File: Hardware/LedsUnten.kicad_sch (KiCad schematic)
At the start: 27 parts

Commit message: assign remaining LCSC numbers and change R_sense of LED drivers
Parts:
- added R9: 0.5, Resistor_SMD:R_0805_2012Metric, symbol Device:R_Small
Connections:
- net GND: now also R9.2
- new net LedTreiber4/R_{sense}: R9.1
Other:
- sheet LedTreiber4 ports: added R_{sense}; removed none
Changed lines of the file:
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@@
 	(wire
 		(pts
-			(xy 88.9 116.84) (xy 201.93 116.84)
+			(xy 95.25 116.84) (xy 201.93 116.84)
 		)
 		(stroke
@@
 	(wire
 		(pts
-			(xy 74.93 97.79) (xy 88.9 97.79)
+			(xy 74.93 93.98) (xy 95.25 93.98)
 		)
 		(stroke
@@
 	(wire
 		(pts
-			(xy 88.9 97.79) (xy 88.9 116.84)
+			(xy 95.25 93.98) (xy 95.25 116.84)
 		)
 		(stroke
@@
 	(wire
 		(pts
-			(xy 105.41 76.2) (xy 105.41 90.17)
+			(xy 74.93 97.79) (xy 87.63 97.79)
 		)
 		(stroke
@@
 		)
 	)
+	(wire
+		(pts
+			(xy 105.41 76.2) (xy 105.41 90.17)
+		)
+		(stroke
+			(width 0)
+			(type default)
+		)
+	)
 	(global_label "WhiteDim"
 		(shape input)
@@
 	)
 	(symbol
+		(lib_id "Device:R_Small")
+		(at 87.63 100.33 0)
+		(unit 1)
+		(exclude_from_sim no)
+		(in_bom yes)
+		(on_board yes)
+		(dnp no)
+		(fields_autoplaced yes)
+		(property "Reference" "R9"
+			(at 90.17 99.0599 0)
+			(effects
+				(font
+					(size 1.27 1.27)
+				)
+				(justify left)
+			)
+		)
+		(property "Value" "0.5"
+			(at 90.17 101.5999 0)
+			(effects
+				(font
+					(size 1.27 1.27)
+				)
+				(justify left)
+			)
+		)
+		(property "Footprint" "Resistor_SMD:R_0805_2012Metric"
+			(at 87.63 100.33 0)
+			(effects
+				(font
+					(size 1.27 1.27)
+				)
+				(hide yes)
+			)
+		)
+		(property "Datasheet" "~"
+			(at 87.63 100.33 0)
+			(effects
+				(font
+					(size 1.27 1.27)
+				)
+				(hide yes)
+			)
+		)
+		(property "Description" "Resistor, small symbol"
+			(at 87.63 100.33 0)
+			(effects
+				(font
+					(size 1.27 1.27)
+				)
+				(hide yes)
+			)
+		)
+		(pin "1"
+		)
+		(pin "2"
+		)
+		(instances
+			(project "LEDTischLampe"
+				(path "/34c772aa-2c68-48ca-93c3-7ad335c6d96d/5ca28fd6-5d3d-44e4-a7e8-e548f0114941"
+					(reference "R9")
+					(unit 1)
+				)
+			)
+		)
+	)
+	(symbol
+		(lib_id "power:GND")
+		(at 87.63 102.87 0)
+		(unit 1)
+		(exclude_from_sim no)
+		(in_bom yes)
+		(on_board yes)
+		(dnp no)
+		(property "Reference" "#PWR025"
+			(at 87.63 109.22 0)
+			(effects
+				(font
+					(size 1.27 1.27)
+				)
+				(hide yes)
+			)
+		)
+		(property "Value" "GND"
+			(at 87.63 106.426 0)
+			(effects
+				(font
+					(size 1.27 1.27)
+				)
+			)
+		)
+		(property "Footprint" ""
+			(at 87.63 102.87 0)
+			(effects
+				(font
+					(size 1.27 1.27)
+				)
+				(hide yes)
+			)
+		)
+		(property "Datasheet" ""
+			(at 87.63 102.87 0)
+			(effects
+				(font
+					(size 1.27 1.27)
+				)
+				(hide yes)
+			)
+		)
+		(property "Description" ""
+			(at 87.63 102.87 0)
+			(effects
+				(font
+					(size 1.27 1.27)
+				)
+				(hide yes)
+			)
+		)
+		(pin "1"
+		)
+		(instances
+			(project "LEDTischLampe"
+				(path "/34c772aa-2c68-48ca-93c3-7ad335c6d96d/5ca28fd6-5d3d-44e4-a7e8-e548f0114941"
+					(reference "#PWR025")
+					(unit 1)
+				)
+			)
+		)
+	)
+	(symbol
 		(lib_id "Device:R")
 		(at 111.76 104.14 90)
@@
 		)
 		(pin "LEDN" input
-			(at 74.93 97.79 0)
+			(at 74.93 93.98 0)
 			(effects
 				(font
@@
 			)
 		)
+		(pin "R_{sense}" input
+			(at 74.93 97.79 0)
+			(effects
+				(font
+					(size 1.27 1.27)
+				)
+				(justify right)
+			)
+		)

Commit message: remove LCSC numbers from silkscreen (bug in jlcpcb-tools)
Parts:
- LED1, LED10, LED11, LED12, LED13, LED14, LED15, LED16, LED17, LED18, LED19, LED2, LED20, LED21, LED22, LED23, LED24, LED3, LED4, LED5, LED6, LED7, LED8, LED9: LCSC (none) -> C210320
- R5, R6, R7: LCSC (none) -> C17415
- R9: LCSC (none) -> C2930328

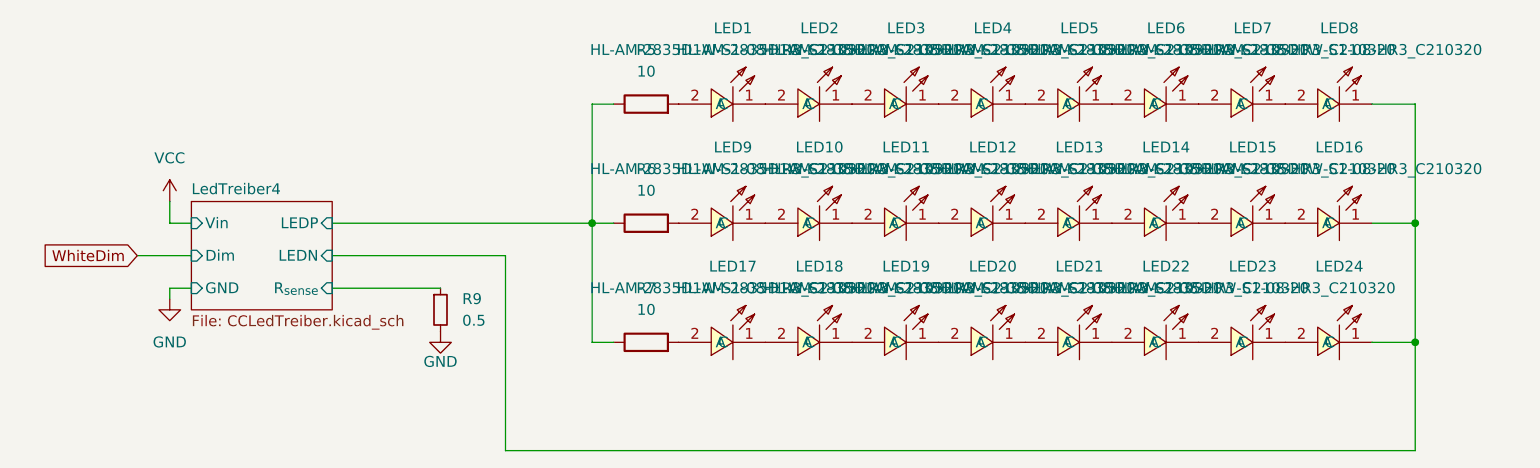
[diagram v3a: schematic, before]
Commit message: some fixes and BOM optimization, heatsinking, etc
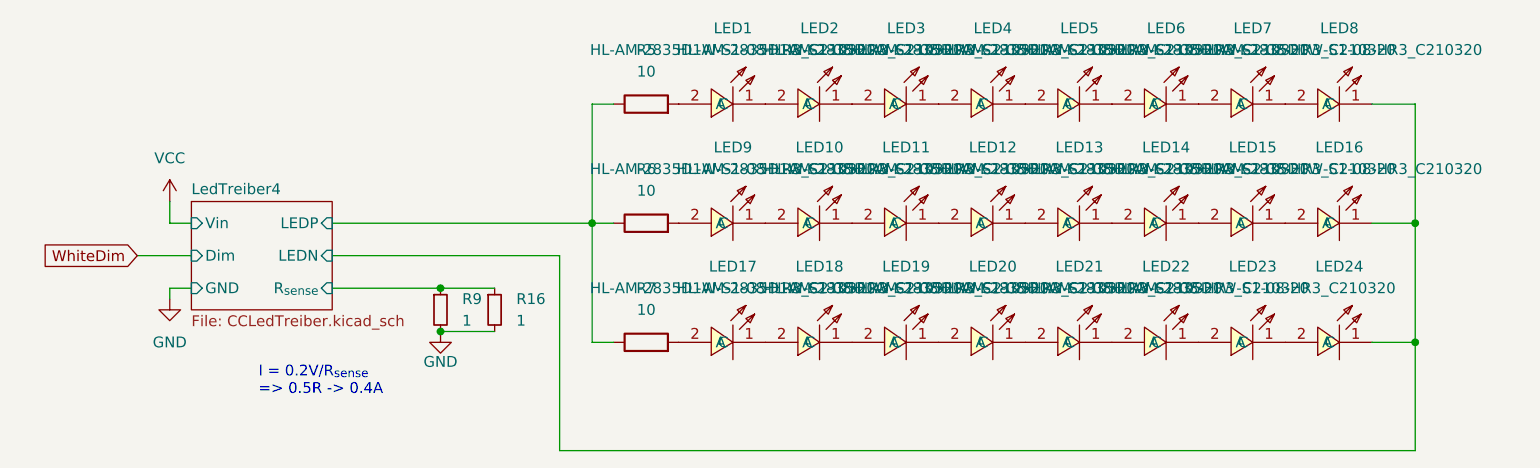
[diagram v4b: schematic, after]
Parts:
- added R16: 1, Resistor_SMD:R_0805_2012Metric, symbol Device:R_Small
- R9: value 0.5 -> 1; LCSC C2930328 -> C25271
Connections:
- net GND: now also R16.2
- net LedTreiber4/R_{sense}: now also R16.1
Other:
- note added: "I = 0.2V/R_{sense} => 0.5R -> 0.4A"
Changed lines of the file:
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@@
 		(color 0 0 0 0)
 	)
+	(junction
+		(at 87.63 102.87)
+		(diameter 0)
+		(color 0 0 0 0)
+	)
+	(junction
+		(at 87.63 97.79)
+		(diameter 0)
+		(color 0 0 0 0)
+	)
 	(wire
 		(pts
@@
 	(wire
 		(pts
-			(xy 95.25 116.84) (xy 201.93 116.84)
+			(xy 101.6 116.84) (xy 201.93 116.84)
 		)
 		(stroke
@@
 	(wire
 		(pts
+			(xy 87.63 97.79) (xy 93.98 97.79)
+		)
+		(stroke
+			(width 0)
+			(type default)
+		)
+	)
+	(wire
+		(pts
 			(xy 55.88 87.63) (xy 55.88 90.17)
 		)
@@
 	(wire
 		(pts
-			(xy 74.93 93.98) (xy 95.25 93.98)
+			(xy 74.93 93.98) (xy 101.6 93.98)
 		)
 		(stroke
@@
 	(wire
 		(pts
-			(xy 95.25 93.98) (xy 95.25 116.84)
+			(xy 101.6 93.98) (xy 101.6 116.84)
 		)
 		(stroke
@@
 	(wire
 		(pts
+			(xy 87.63 102.87) (xy 93.98 102.87)
+		)
+		(stroke
+			(width 0)
+			(type default)
+		)
+	)
+	(wire
+		(pts
 			(xy 201.93 104.14) (xy 201.93 90.17)
 		)
@@
 			(width 0)
 			(type default)
+		)
+	)
+	(text "I = 0.2V/R_{sense}\n=> 0.5R -> 0.4A"
+		(exclude_from_sim no)
+		(at 66.294 108.712 0)
+		(effects
+			(font
+				(size 1.27 1.27)
+			)
+			(justify left)
 		)
 	)
@@
 			)
 		)
-		(property "Value" "0.5"
+		(property "Value" "1"
 			(at 90.17 101.5999 0)
 			(effects
@@
 			)
 		)
-		(property "LCSC" "C2930328"
+		(property "LCSC" "C25271"
 			(at 90.17 99.0599 0)
 			(effects
@@
 					(unit 1)
 				)
+			)
+		)
+	)
+	(symbol
+		(lib_id "Device:R_Small")
+		(at 93.98 100.33 0)
+		(unit 1)
+		(exclude_from_sim no)
+		(in_bom yes)
+		(on_board yes)
+		(dnp no)
+		(fields_autoplaced yes)
+		(property "Reference" "R16"
+			(at 96.52 99.0599 0)
+			(effects
+				(font
+					(size 1.27 1.27)
+				)
+				(justify left)
+			)
+		)
+		(property "Value" "1"
+			(at 96.52 101.5999 0)
+			(effects
+				(font
+					(size 1.27 1.27)
+				)
+				(justify left)
+			)
+		)
+		(property "Footprint" "Resistor_SMD:R_0805_2012Metric"
+			(at 93.98 100.33 0)
+			(effects
+				(font
+					(size 1.27 1.27)
+				)
+				(hide yes)
+			)
+		)
+		(property "Datasheet" "~"
+			(at 93.98 100.33 0)
+			(effects
+				(font
+					(size 1.27 1.27)
+				)
+				(hide yes)
+			)
+		)
+		(property "Description" "Resistor, small symbol"
+			(at 93.98 100.33 0)
+			(effects
+				(font
+					(size 1.27 1.27)
+				)
+				(hide yes)
+			)
+		)
+		(property "LCSC" "C25271"
+			(at 96.52 99.0599 0)
+			(effects
+				(font
+					(size 1.27 1.27)
+				)
+				(hide yes)
+			)
+		)
+		(pin "1"
+		)
+		(pin "2"
+		)
+		(instances
+			(project "LEDTischLampe"
+				(path "/34c772aa-2c68-48ca-93c3-7ad335c6d96d/5ca28fd6-5d3d-44e4-a7e8-e548f0114941"
+					(reference "R16")
+					(unit 1)
+				)

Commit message: final touches for v1.0
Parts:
- LED1, LED10, LED11, LED12, LED13, LED14, LED15, LED16, LED17, LED18, LED19, LED2, LED20, LED21, LED22, LED23, LED24, LED3, LED4, LED5, LED6, LED7, LED8, LED9: LCSC C210320 -> (none)
- R16, R9: LCSC C25271 -> (none)
- R5, R6, R7: LCSC C17415 -> (none)

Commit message: some more tweaks (rotated input terminal block, added voltage measurement)
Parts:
- LED1, LED10, LED11, LED12, LED13, LED14, LED15, LED16, LED17, LED18, LED19, LED2, LED20, LED21, LED22, LED23, LED24, LED3, LED4, LED5, LED6, LED7, LED8, LED9: LCSC Part C210320 -> (none)
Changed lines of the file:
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@@
-			)
-		)
-		(property "LCSC Part" "C210320"
-			(at 130.81 77.47 0)
-			(effects
-				(font
-					(size 1.27 1.27)
-				)
-				(hide yes)
 			)
 		)
@@
 			)
 		)
-		(property "LCSC Part" "C210320"
-			(at 140.97 63.5 0)
-			(effects
-				(font
-					(size 1.27 1.27)
-				)
-				(hide yes)
-			)
-		)
 		(pin "2"
 		)
@@
 			)
 		)
-		(property "LCSC Part" "C210320"
-			(at 120.65 77.47 0)
-			(effects
-				(font
-					(size 1.27 1.27)
-				)
-				(hide yes)
-			)
-		)
 		(pin "2"
 		)
@@
 			)
 		)
-		(property "LCSC Part" "C210320"
-			(at 120.65 63.5 0)
-			(effects
-				(font
-					(size 1.27 1.27)
-				)
-				(hide yes)
-			)
-		)
 		(pin "2"
 		)
@@
 			)
 		)
-		(property "LCSC Part" "C210320"
-			(at 181.61 91.44 0)
-			(effects
-				(font
-					(size 1.27 1.27)
-				)
-				(hide yes)
-			)
-		)
 		(pin "2"
 		)
@@
 			)
 		)
-		(property "LCSC Part" "C210320"
-			(at 130.81 63.5 0)
-			(effects
-				(font
-					(size 1.27 1.27)
-				)
-				(hide yes)
-			)
-		)
 		(pin "2"
 		)
@@
 			)
 		)
-		(property "LCSC Part" "C210320"
-			(at 181.61 77.47 0)
-			(effects
-				(font
-					(size 1.27 1.27)
-				)
-				(hide yes)
-			)
-		)
 		(pin "2"
 		)
@@
 			)
 		)
-		(property "LCSC Part" "C210320"
-			(at 161.29 77.47 0)
-			(effects
-				(font
-					(size 1.27 1.27)
-				)
-				(hide yes)
-			)
-		)
 		(pin "2"
 		)
@@
 			)
 		)
-		(property "LCSC Part" "C210320"
-			(at 161.29 91.44 0)
-			(effects
-				(font
-					(size 1.27 1.27)
-				)
-				(hide yes)
-			)
-		)
 		(pin "2"
 		)
@@
 			)
 		)
-		(property "LCSC Part" "C210320"
-			(at 161.29 63.5 0)
-			(effects
-				(font
-					(size 1.27 1.27)
-				)
-				(hide yes)
-			)
-		)
 		(pin "2"
 		)
@@
 			)
 		)
-		(property "LCSC Part" "C210320"
-			(at 171.45 91.44 0)
-			(effects
-				(font
-					(size 1.27 1.27)
-				)
-				(hide yes)
-			)
-		)
 		(pin "2"
 		)
@@
 			)
 		)
-		(property "LCSC Part" "C210320"
-			(at 140.97 77.47 0)
-			(effects
-				(font
-					(size 1.27 1.27)
-				)
-				(hide yes)
-			)
-		)
 		(pin "2"
 		)
@@
 			)
 		)
-		(property "LCSC Part" "C210320"
-			(at 151.13 91.44 0)
-			(effects
-				(font
-					(size 1.27 1.27)
-				)
-				(hide yes)
-			)
-		)
 		(pin "2"
 		)
@@
 			)
 		)
-		(property "LCSC Part" "C210320"
-			(at 171.45 63.5 0)
-			(effects
-				(font
-					(size 1.27 1.27)
-				)
-				(hide yes)
-			)
-		)
 		(pin "2"
 		)
@@
 			)
 		)
-		(property "LCSC Part" "C210320"
-			(at 181.61 63.5 0)
-			(effects
-				(font
-					(size 1.27 1.27)
-				)
-				(hide yes)
-			)
-		)
 		(pin "2"
 		)
@@
 			)
 		)
-		(property "LCSC Part" "C210320"
-			(at 191.77 63.5 0)
-			(effects
-				(font
-					(size 1.27 1.27)
-				)
-				(hide yes)
-			)
-		)
 		(pin "2"
 		)
@@
 			)
 		)
-		(property "LCSC Part" "C210320"
-			(at 140.97 91.44 0)
-			(effects
-				(font
-					(size 1.27 1.27)
-				)
-				(hide yes)
-			)
-		)
 		(pin "2"
 		)
@@
 			)
 		)
-		(property "LCSC Part" "C210320"
-			(at 120.65 91.44 0)
-			(effects
-				(font
-					(size 1.27 1.27)
-				)
-				(hide yes)
-			)
-		)
 		(pin "2"
 		)
@@
 			)
 		)
-		(property "LCSC Part" "C210320"
-			(at 151.13 63.5 0)
-			(effects
-				(font
-					(size 1.27 1.27)
-				)
-				(hide yes)
-			)
-		)
 		(pin "2"
 		)
@@
 			)
 		)
-		(property "LCSC Part" "C210320"
-			(at 191.77 91.44 0)
-			(effects
-				(font
-					(size 1.27 1.27)
-				)
-				(hide yes)
-			)
-		)
 		(pin "2"
 		)
@@
 			)
 		)
-		(property "LCSC Part" "C210320"
-			(at 171.45 77.47 0)
-			(effects
-				(font
-					(size 1.27 1.27)
-				)
-				(hide yes)
-			)
-		)
 		(pin "2"
 		)
@@
 			)
 		)
-		(property "LCSC Part" "C210320"
-			(at 130.81 91.44 0)
-			(effects
-				(font
-					(size 1.27 1.27)
-				)
-				(hide yes)
-			)
-		)
 		(pin "2"
 		)
@@
 			)
 		)
-		(property "LCSC Part" "C210320"
-			(at 151.13 77.47 0)
-			(effects
-				(font
-					(size 1.27 1.27)
-				)
-				(hide yes)
-			)
-		)
 		(pin "2"
 		)
@@
 			(effects
 				(font
-					(size 1.27 1.27)
-				)
-				(hide yes)
-			)
-		)
-		(property "LCSC Part" "C210320"
-			(at 191.77 77.47 0)
-			(effects
-				(font
